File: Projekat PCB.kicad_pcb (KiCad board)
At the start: 2 copper layers, 106 x 110 mm, 84 parts, among them J1 PJ-002A, J3 MSD-3-A, J4 MD-30SM, P1 ICSP, P2 LCD-H, P3 USB_B, SW1 SW_SPST, U1 LM334Z, U2 LM317T_TO220, U3 MCP6022-I/SN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

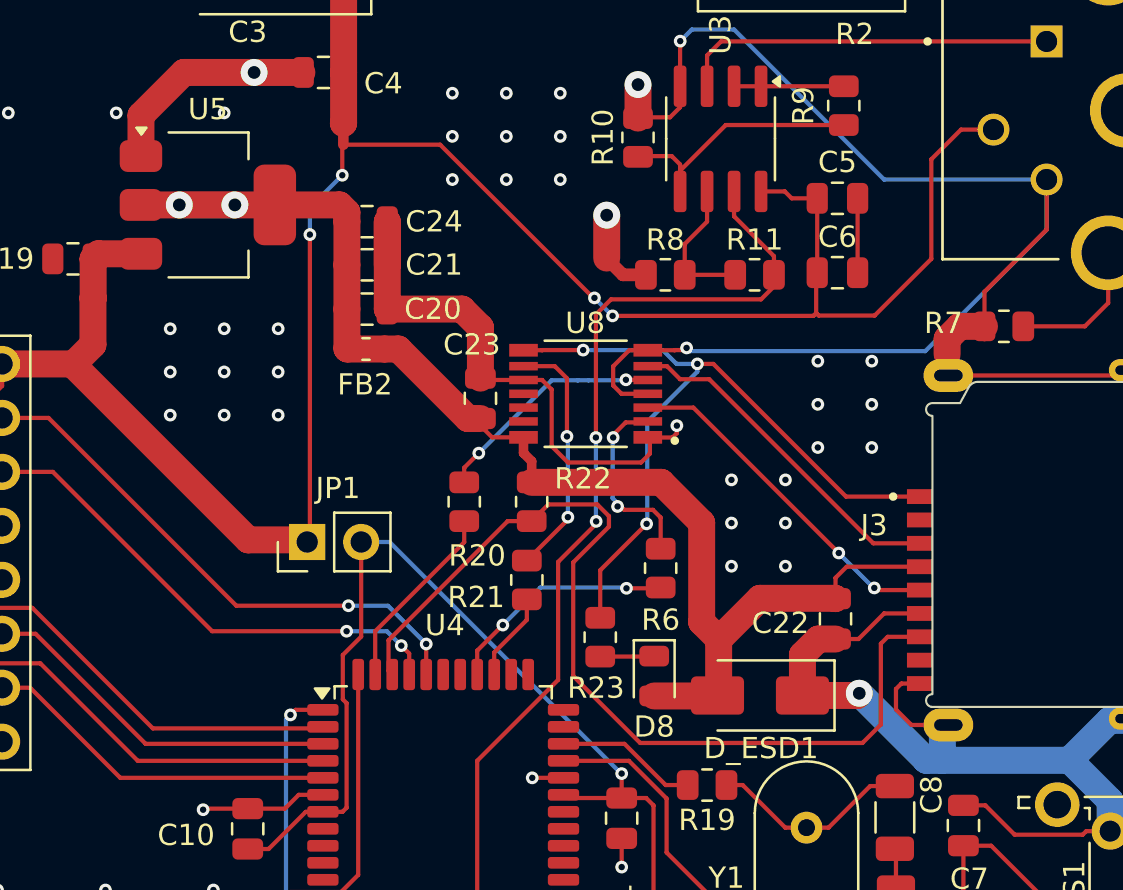
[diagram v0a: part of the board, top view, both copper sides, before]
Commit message: Zamena Buffer-a sa LevelShifter-om
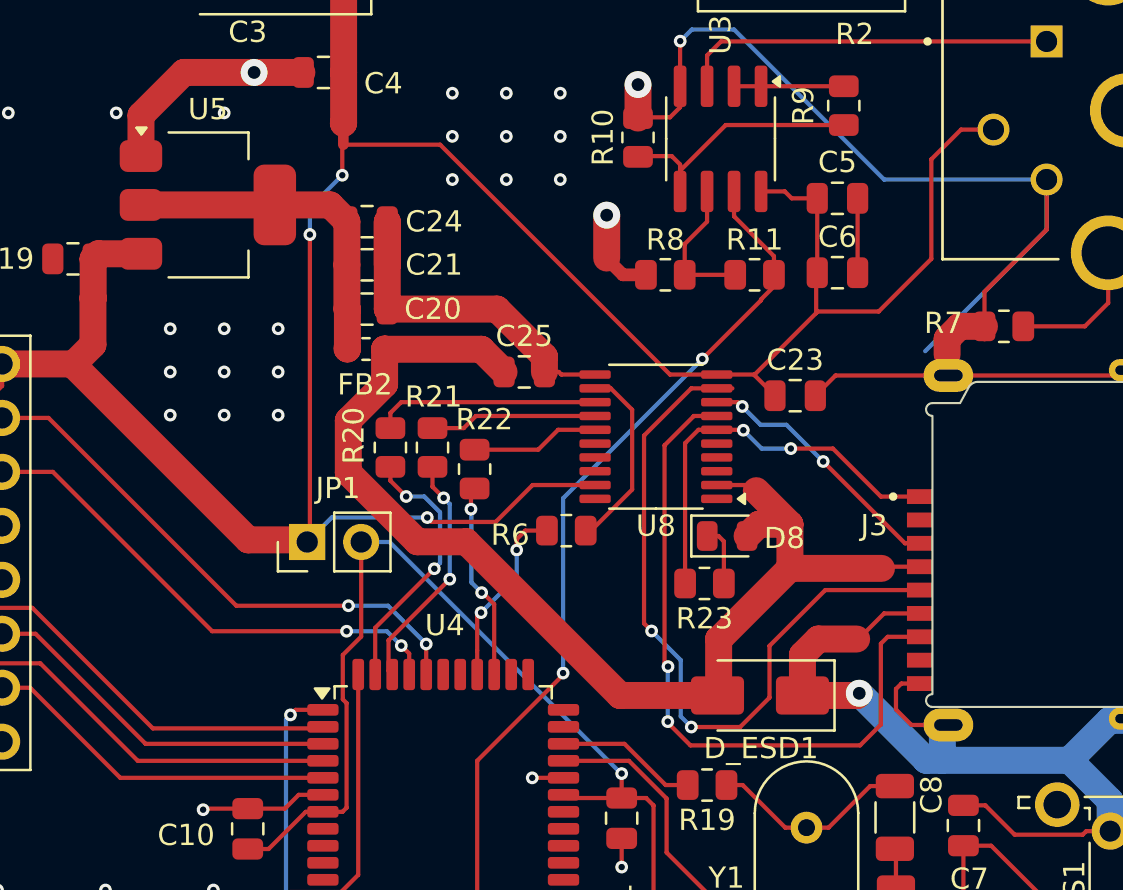
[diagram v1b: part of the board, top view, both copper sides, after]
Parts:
- removed C22: 100nF, Capacitor_SMD:C_0805_2012Metric
- added C25: 100nF, Capacitor_SMD:C_0805_2012Metric, F.Cu at (115.2, 95.0)
- J3: value MSD-3-A -> MSD-3-A MicroSD card socket
- R22: value 10k -> 1k
- R23: value 470 -> 1k
- U8: value 74LVC125 -> TXS0108EPW; footprint 74LVC125APW_118:IC_74LVC125APW,118 -> Package_SO:TSSOP-20_4.4x6.5mm_P0.65mm
- moved C23 14.8 mm to (128.0, 96.1), turned to 0 degrees
- moved R21 7.66 mm to (110.9, 98.6)
- moved D8 7.43 mm to (124.8, 102.7), turned to 0 degrees
- moved R23 5.52 mm to (123.7, 105.0), turned to 180 degrees
- moved R6 4.78 mm to (117.2, 102.5), turned to 0 degrees
- moved R20 4.31 mm to (108.9, 98.6)
- moved U8 3.87 mm to (121.4, 98.0)
- moved R22 3.10 mm to (112.9, 99.6)
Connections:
- C20 pad 1: /MicroSD card reader/3.3V -> Net-(U5-VO)
- C21 pad 1: /MicroSD card reader/3.3V -> Net-(U5-VO)
- C23 pad 1: /MicroSD card reader/3.3V -> VCC
- C24 pad 1: /MicroSD card reader/3.3V -> Net-(U5-VO)
- FB2 pad 1: /MicroSD card reader/3.3V -> Net-(U5-VO)
- J3 pad 7: /MicroSD card reader/MISO -> Net-(J3-DAT0)
- R20 pad 2: Net-(U8-2A) -> Net-(U8-B7)
- R21 pad 1: /MicroSD card reader/CS -> /MicroSD card reader/MISO
- R21 pad 2: Net-(U8-3A) -> Net-(U8-B6)
- R22 pad 1: /MicroSD card reader/MISO -> /MicroSD card reader/CS
- R22 pad 2: /MicroSD card reader/3.3V -> Net-(U8-B5)
- R23 pad 1: Net-(J3-DAT2) -> Net-(D8-K)
- R23 pad 2: Net-(D8-K) -> Net-(J3-DAT2)
- R6 pad 2: Net-(U8-1A) -> Net-(U8-B8)
- U5 pad 2: /MicroSD card reader/3.3V -> Net-(U5-VO)
- U8 pad 1: GND -> unconnected-(U8-A1-Pad1)
- U8 pad 10: GND -> VCC
- U8 pad 11: unconnected-(U8-4Y-Pad11) -> GND
- U8 pad 12: unconnected-(U8-4A-Pad12) -> Net-(U8-B8)
- U8 pad 13: unconnected-(U8-4~{OE}-Pad13) -> Net-(U8-B7)
- U8 pad 14: /MicroSD card reader/3.3V -> Net-(U8-B6)
- U8 pad 2: Net-(U8-1A) -> /MicroSD card reader/3.3V
- U8 pad 3: Net-(J3-CLK) -> unconnected-(U8-A2-Pad3)
- U8 pad 4: GND -> unconnected-(U8-A3-Pad4)
- U8 pad 5: Net-(U8-2A) -> unconnected-(U8-A4-Pad5)
- U8 pad 6: Net-(J3-CMD) -> Net-(J3-DAT2)
- U8 pad 7: GND -> Net-(J3-DAT0)
- U8 pad 8: Net-(J3-DAT2) -> Net-(J3-CMD)
- U8 pad 9: Net-(U8-3A) -> Net-(J3-CLK)
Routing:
- net /MicroSD card reader/MISO: track 45.1 -> 11.4 mm, vias 0 -> 2
- net Net-(J3-DAT0): track 0.00 -> 32.8 mm, vias 0 -> 2
- net GND: track 225.4 -> 204.6 mm, vias 116 -> 102
- net VCC: track 186.6 -> 205.0 mm, vias 5 -> 4
- net Net-(J3-CLK): track 16.4 -> 34.7 mm
- net Net-(J3-DAT2): track 35.6 -> 19.2 mm, vias 3 -> 2
- net Net-(U5-VO): track 0.00 -> 16.1 mm
- net Net-(U8-3A): track 11.5 -> 0.00 mm, vias 2 -> 0
- net Net-(U8-2A): track 11.1 -> 0.00 mm, vias 2 -> 0
- net Net-(U8-B7): track 0.00 -> 10.6 mm
- net Net-(U8-1A): track 9.08 -> 0.00 mm, vias 2 -> 0
- net Net-(U8-B8): track 0.00 -> 8.90 mm
- net Net-(U8-B6): track 0.00 -> 7.89 mm
- net /MicroSD card reader/3.3V: track 63.6 -> 56.9 mm, vias 2 -> 0
- net Net-(U8-B5): track 0.00 -> 6.06 mm
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
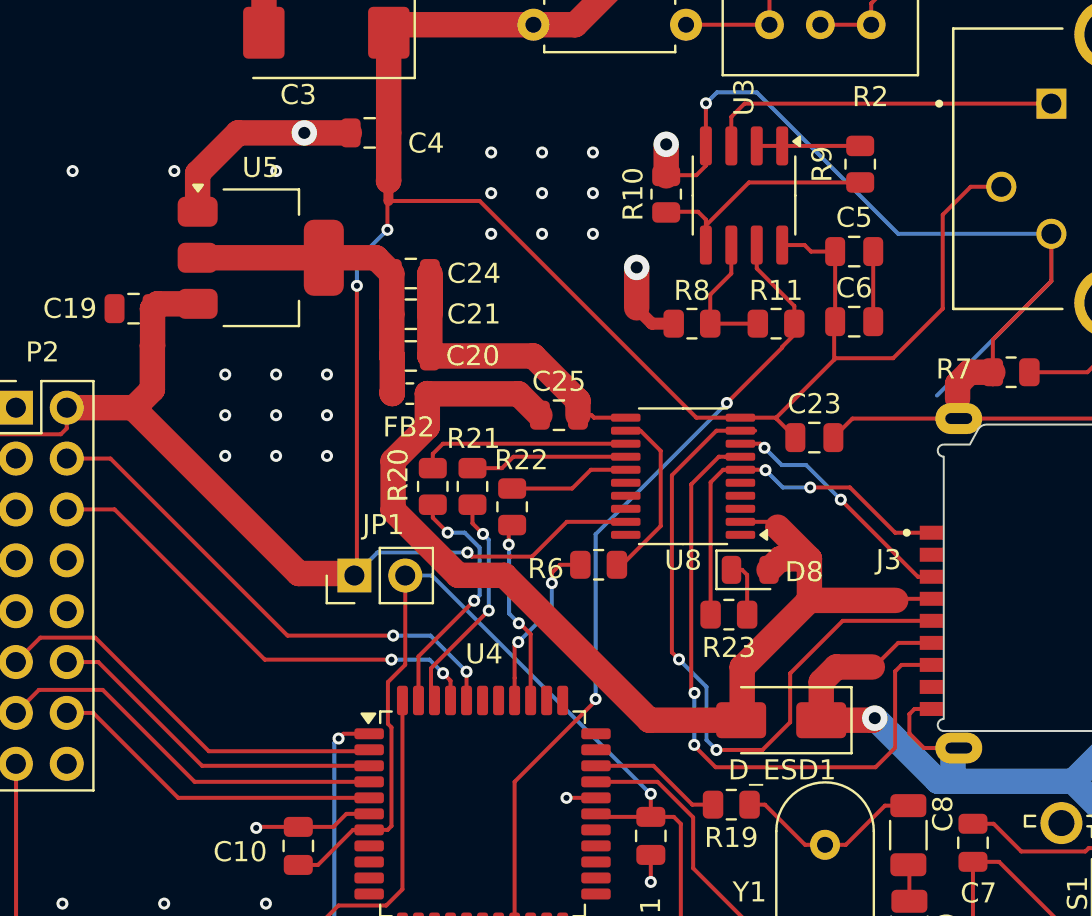
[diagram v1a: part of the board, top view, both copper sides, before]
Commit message: Popravka rutiranja Level Shifter-a
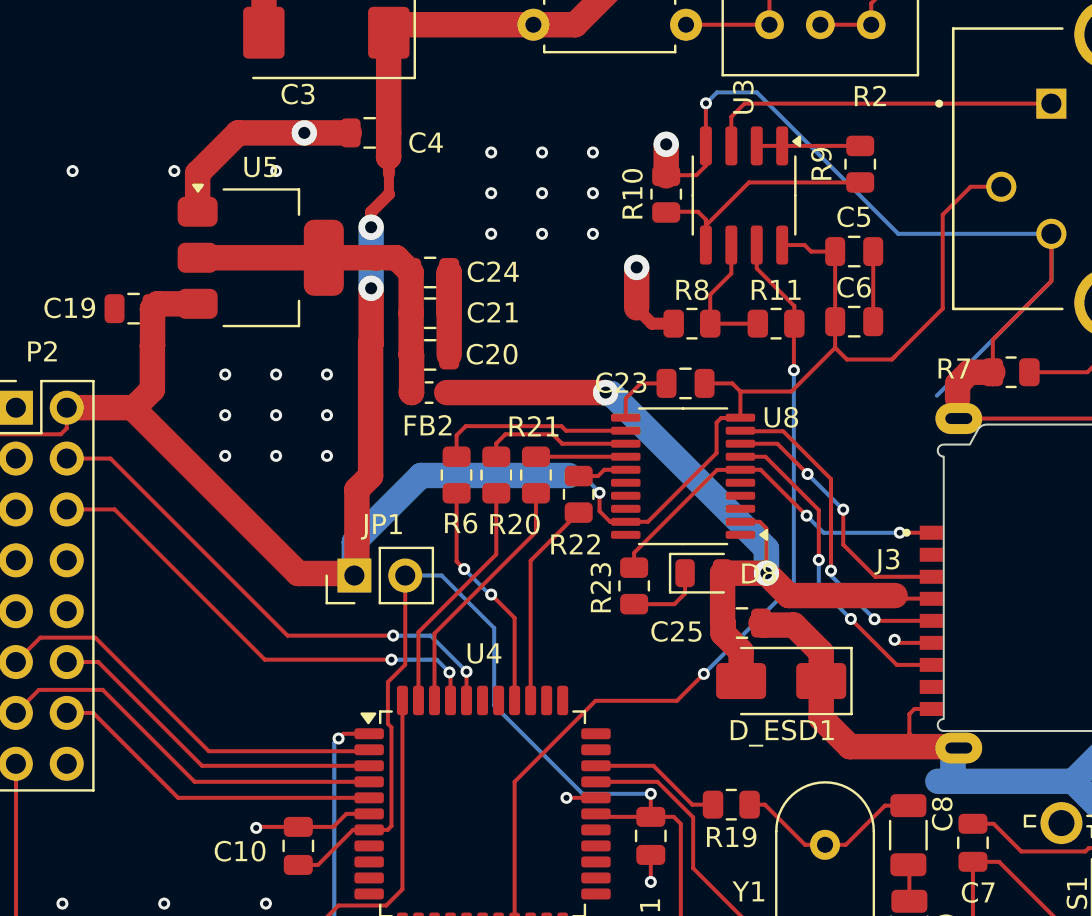
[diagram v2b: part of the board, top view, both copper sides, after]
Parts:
- moved C25 13.8 mm to (124.4, 105.4)
- moved R6 8.39 mm to (110.1, 98.0), turned to 90 degrees
- moved C23 6.98 mm to (121.5, 93.4), turned to 180 degrees
- moved R23 4.94 mm to (119.0, 103.5), turned to 90 degrees
- moved R22 3.38 mm to (116.2, 98.9)
- moved R20 3.22 mm to (112.1, 98.0)
- moved R21 3.22 mm to (114.1, 98.0)
- moved D8 2.32 mm to (122.4, 102.9)
- moved D_ESD1 1.96 mm to (126.3, 108.3)
- moved C21 0.97 mm to (108.8, 89.9)
- moved C20 0.97 mm to (108.8, 92.0)
- moved C24 0.97 mm to (108.8, 87.9)
- moved FB2 0.97 mm to (108.7, 93.9)
- moved NT1 0.35 mm to (106.7, 83.5)
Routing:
- net Net-(J3-CLK): track 34.7 -> 16.4 mm
- net Net-(J3-DAT0): track 32.8 -> 16.1 mm
- net /MicroSD card reader/3.3V: track 56.9 -> 40.8 mm, vias 0 -> 2
- net GND: track 204.6 -> 190.6 mm
- net VCC: track 205.0 -> 196.7 mm
- net Net-(U8-B5): track 6.06 -> 2.48 mm
- net Net-(U8-B6): track 7.89 -> 4.48 mm
- net Net-(U8-B7): track 10.6 -> 7.51 mm
- net /MicroSD card reader/CLK: track 8.73 -> 11.6 mm
- net /Microcontroller/S_OUT: track 40.7 -> 43.1 mm
- net VDD: track 54.7 -> 57.0 mm
- net /MicroSD card reader/MISO: track 11.4 -> 12.4 mm, vias 2 -> 0
- net /MicroSD card reader/CS: track 9.31 -> 10.4 mm, vias 2 -> 0
- net Net-(J3-CMD): track 12.3 -> 13.3 mm
- net Net-(U5-VO): track 16.1 -> 17.0 mm
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
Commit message: gitignore
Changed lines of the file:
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@@
 	)
 	(segment
+		(start 123.0834 96.8886)
+		(end 123.0834 95.3646)
+		(width 0.2)
+		(layer "F.Cu")
+		(net 10)
+	)
+	(segment
 		(start 127.8026 86.825)
 		(end 129.005 86.825)
@@
 	)
 	(segment
-		(start 123.312 95.136)
-		(end 124.2575 95.136)
-		(width 0.2)
-		(layer "F.Cu")
-		(net 10)
-	)
-	(segment
 		(start 127.4776 86.5)
 		(end 127.8026 86.825)
@@
 	)
 	(segment
-		(start 118.5495 100.319)
-		(end 118.5509 100.3176)
+		(start 118.5509 100.3176)
+		(end 119.6544 100.3176)
 		(width 0.2)
 		(layer "F.Cu")
@@
 	)
 	(segment
-		(start 119.6544 100.3176)
-		(end 123.0834 96.8886)
-		(width 0.2)
-		(layer "F.Cu")
-		(net 10)
-	)
-	(segment
 		(start 94.9148 91.5292)
 		(end 94.9148 93.7136)
@@
 	)
 	(segment
-		(start 118.5509 100.3176)
-		(end 119.6544 100.3176)
+		(start 123.312 95.136)
+		(end 124.2575 95.136)
 		(width 0.2)
 		(layer "F.Cu")
@@
 	)
 	(segment
+		(start 123.0834 95.3646)
+		(end 123.312 95.136)
+		(width 0.2)
+		(layer "F.Cu")
+		(net 10)
+	)
+	(segment
 		(start 129.005 91.6274)
 		(end 126.8199 93.8125)
@@
 	)
 	(segment
-		(start 123.0834 95.3646)
-		(end 123.312 95.136)
-		(width 0.2)
-		(layer "F.Cu")
-		(net 10)
-	)
-	(segment
 		(start 131.9677 92.0823)
 		(end 131.8988 92.1512)
@@
 	)
 	(segment
+		(start 124.2575 95.136)
+		(end 124.2745 95.119)
+		(width 0.2)
+		(layer "F.Cu")
+		(net 10)
+	)
+	(segment
 		(start 122.484 93.4088)
 		(end 123.8708 93.4088)
@@
 	)
 	(segment
+		(start 119.6544 100.3176)
+		(end 123.0834 96.8886)
+		(width 0.2)
+		(layer "F.Cu")
+		(net 10)
+	)
+	(segment
 		(start 105.8368 85.611)
 		(end 105.8368 84.849)
@@
 	)
 	(segment
-		(start 124.2575 95.136)
-		(end 124.2745 95.119)
-		(width 0.2)
-		(layer "F.Cu")
-		(net 10)
-	)
-	(segment
 		(start 135.7724 83.59)
 		(end 134.375 84.9874)
@@
 	)
 	(segment
-		(start 123.0834 96.8886)
-		(end 123.0834 95.3646)
-		(width 0.2)
-		(layer "F.Cu")
-		(net 10)
-	)
-	(segment
 		(start 105 103)
 		(end 104.600805 102.600805)
@@
 		(net 10)
 	)
+	(segment
+		(start 118.5495 100.319)
+		(end 118.5509 100.3176)
+		(width 0.2)
+		(layer "F.Cu")
+		(net 10)
+	)
 	(via
 		(at 105.8368 85.611)
@@
 	)
 	(segment
-		(start 117.5462 93.866)
-		(end 109.6074 93.866)
-		(width 1.27)
-		(layer "F.Cu")
-		(net 82)
-	)
-	(segment
 		(start 124.3092 108.2678)
 		(end 124.3003 108.2589)
@@
 	)
 	(segment
+		(start 117.5462 93.866)
+		(end 109.6074 93.866)
+		(width 1.27)
+		(layer "F.Cu")
+		(net 82)
+	)
+	(segment
 		(start 125.5726 100.6478)
 		(end 125.2438 100.319)
@@
 	)
 	(segment
-		(start 125.5726 101.6638)
-		(end 125.5726 102.883)
-		(width 1.27)
-		(layer "B.Cu")
-		(net 82)
-	)
-	(segment
 		(start 117.5462 93.866)
-		(end 117.597 93.9168)
+		(end 125.5726 101.8924)
 		(width 1.27)
 		(layer "B.Cu")
@@
 	)
 	(segment
-		(start 117.597 93.9168)
-		(end 117.8256 93.9168)
-		(width 1.27)
-		(layer "B.Cu")
-		(net 82)
-	)
-	(segment
-		(start 117.8256 93.9168)
-		(end 125.5726 101.6638)
+		(start 125.5726 101.8924)
+		(end 125.5726 102.883)
 		(width 1.27)
 		(layer "B.Cu")
@@
 	)
 	(segment
-		(start 127.63 97.93)
-		(end 126.119 96.419)
+		(start 131.0102 103.0628)
+		(end 133.8276 103.0628)
 		(width 0.2)
 		(layer "F.Cu")
@@
 	)
 	(segment
-		(start 131.0102 103.0628)
-		(end 133.8276 103.0628)
+		(start 128.1507 98.4507)
+		(end 126.119 96.419)
 		(width 0.2)
 		(layer "F.Cu")
@@
 	)
 	(via
-		(at 127.63 97.93)
+		(at 128.1507 98.4507)
 		(size 0.6)
 		(drill 0.3)
@@
 	(segment
 		(start 129.408 99.708)
-		(end 127.63 97.93)
+		(end 128.1507 98.4507)
 		(width 0.2)
 		(layer "B.Cu")
